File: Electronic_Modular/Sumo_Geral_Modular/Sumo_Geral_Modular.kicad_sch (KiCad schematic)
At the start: 50 parts, among them J1 Bateria, J10 ESC1, J11 ESC2, J12 USB_B_Micro, J13 ADSN-9500, J14 PS ADSN-9500, J15 MPU-6050, J2 VL53L0X 1, J3 VL53L0X 2, J4 VL53L0X 3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

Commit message: chore: schamatic review
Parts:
- C8: value C_Polarized -> 100nF
- J14: value PS ADSN-9500 -> ADSN-9500-PS
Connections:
- net 3V3: now also R1.1, R14.2, R2.1; no longer R1.2, R14.1, R2.2
- net EN: now also R14.1; no longer R14.2
- net GND: now also ESP1.38 (GND), H_Bridge1.3 (GND), H_Bridge1.9 (GND)
- net SCL: now also R1.2; no longer R1.1
- net SDA: now also R2.2; no longer R2.1
- net 2s renamed BAT
- no-connect marks 25 -> 22
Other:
- note added: "BOOT"
- note added: "DISTANCE SENSORS"
- note added: "FOR BRUSHED MOTORS"
- note added: "FOR BRUSHLESS MOTORS"
- note added: "IMU SENSOR"
- note added: "IR SENSOR FOR JUDGE COMMANDS"
- note added: "MOUSE SENSOR AND POWER-SOURCE (PS) TO THE MOUSE SENSOR"
- note added: "PULL-UP FOR I2C COMMUNICATION"
- note added: "RESET"
- note added: "VOLTAGE DIVIDER"
- company: (none) -> PROJECT NEON
- title: (none) -> MODULAR PCB FOR MINI SUMO ROBOTS
- moved on the sheet: C1, C2, C3, C4, C5, C6, C7, C8, D2, D3, D4, D5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

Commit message: chore: finish PCB V1
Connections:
- net I00 is gone; now on net IO0: C6.1, R9.1, SW3.1
- net AIN1: now also ESP1.10 (IO25); no longer ESP1.13 (IO14)
- net AIN2: now also ESP1.16 (IO13); no longer ESP1.10 (IO25)
- net BIN2: now also ESP1.14 (IO12); no longer ESP1.12 (IO27)
- net DDT: now also ESP1.6 (IO34); no longer ESP1.5 (SensorVN/39)
- net ESC 1: now also ESP1.12 (IO27); no longer ESP1.14 (IO12)
- net ESC 2: now also ESP1.13 (IO14); no longer ESP1.16 (IO13)
- net INT: now also ESP1.7 (IO35); no longer ESP1.6 (IO34)
- net IR: now also ESP1.5 (SensorVN/39); no longer ESP1.7 (IO35)

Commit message: chore: update PCB and schematic
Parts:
- removed C8: 100nF, Capacitor_SMD:C_0603_1608Metric, symbol Device:C_Polarized
- added C10, C8, C9: 100nF, Capacitor_SMD:C_0603_1608Metric, symbol Device:C
- added J6: EXT2, Connector_PinHeader_2.00mm:PinHeader_1x03_P2.00mm_Vertical, symbol Connector_Generic:Conn_01x03
- added J7: EXT1, Connector_PinHeader_2.00mm:PinHeader_1x03_P2.00mm_Vertical, symbol Connector_Generic:Conn_01x03
- C7: value 100uF -> 100nF
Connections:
- net 3V3: now also C10.1, C9.1, J6.1 (Pin_1), J7.1 (Pin_1)
- net AIN1: now also ESP1.11 (IO26); no longer ESP1.10 (IO25)
- net AIN2: now also ESP1.10 (IO25); no longer ESP1.16 (IO13)
- net DDT: now also ESP1.9 (IO33); no longer ESP1.6 (IO34)
- net EN: now also C8.1
- net GND: now also ESP1.15 (GND), ESP1.39 (GND), C10.2, C8.2, C9.2, J6.3 (Pin_3), J7.3 (Pin_3)
- net INT: now also ESP1.8 (IO32); no longer ESP1.7 (IO35)
- net MOTION: now also ESP1.16 (IO13); no longer ESP1.23 (IO15)
- net BIN1 renamed BIN1/ESC1
- net BIN1/ESC1: now also ESP1.13 (IO14), J10.1 (Pin_1); no longer ESP1.11 (IO26)
- net BIN2: no longer names the net of ESP1.14 (IO12)
- net BIN2: no longer H_Bridge1.11 (BIN2)
- net ESC 1 renamed BIN2/ESC2
- net BIN2/ESC2: now also H_Bridge1.11 (BIN2), J11.1 (Pin_1); no longer J10.1 (Pin_1)
- removed net ESC 2: ESP1.13 (IO14), J11.1 (Pin_1)
- new net IO34: ESP1.6 (IO34), J6.2 (Pin_2)
- new net IO35: ESP1.7 (IO35), J7.2 (Pin_2)
- no-connect marks 22 -> 21
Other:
- moved on the sheet: C5, C6, D3, R1, R14, R2, R8

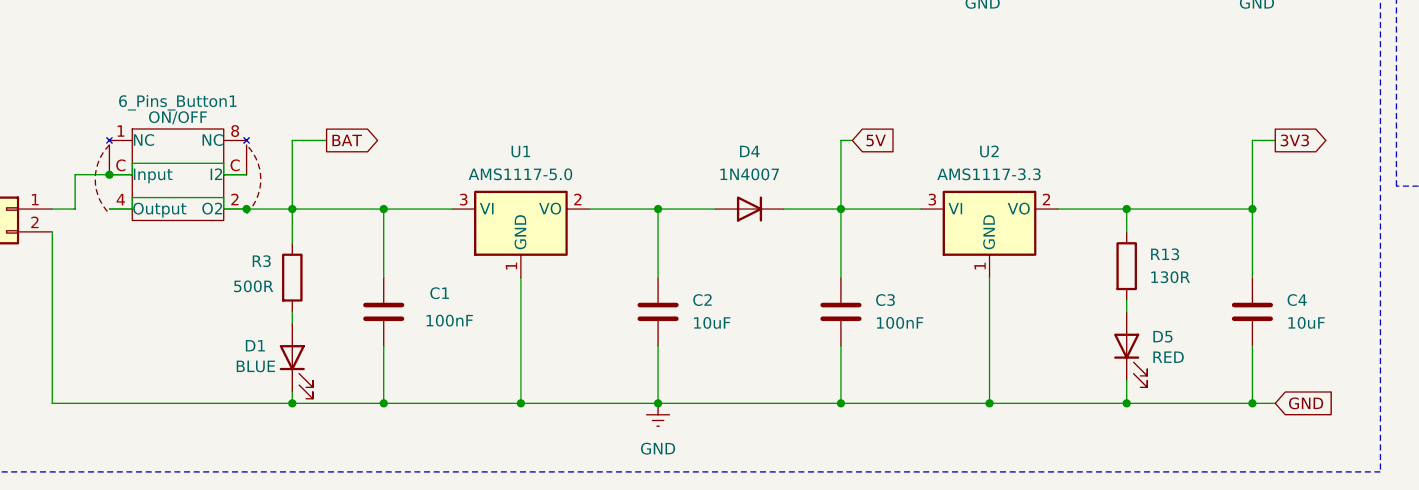
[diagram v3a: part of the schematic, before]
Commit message: chore: update resistors values
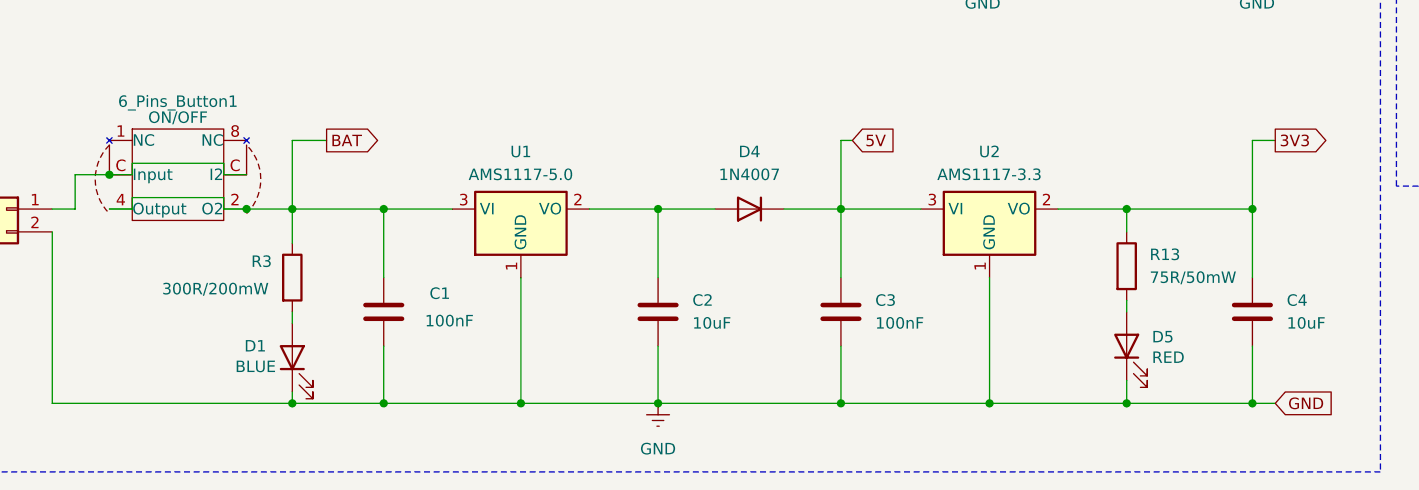
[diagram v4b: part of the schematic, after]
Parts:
- R13: value 130R -> 75R/50mW
- R3: value 500R -> 300R/200mW
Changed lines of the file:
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@@
 			)
 		)
-		(property "Value" "500R"
-			(at 48.006 176.276 0)
+		(property "Value" "300R/200mW"
+			(at 40.132 176.53 0)
 			(effects
 				(font
@@
 			)
 		)
-		(property "Value" "130R"
+		(property "Value" "75R/50mW"
 			(at 149.86 175.2599 0)
 			(effects
